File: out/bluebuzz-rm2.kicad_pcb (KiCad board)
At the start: 6 copper layers, 28 x 44 mm, 109 parts, among them J1 USB-C, J2 BAT, J3 SWD, J4 MOT, J5 TP, J6 PROBE, Q1 AO3400A, Q2 AO3400A, Q3 2N7002, SW1 PWR, U1 RP2350A, U10 USBLC6-2P6, U11 TPS22918DBVR, U2 BQ24074RGT, U20 DPS368, U21 DPS368, U22 DPS368, U23 DPS368, U24 DPS368, U3 TLV75533PDBV, U30 LSM6DS3TR-C, U5 TPS22918DBVR, U6 W25Q32JVUUIQ, U7 RM2, Y1 12MHz

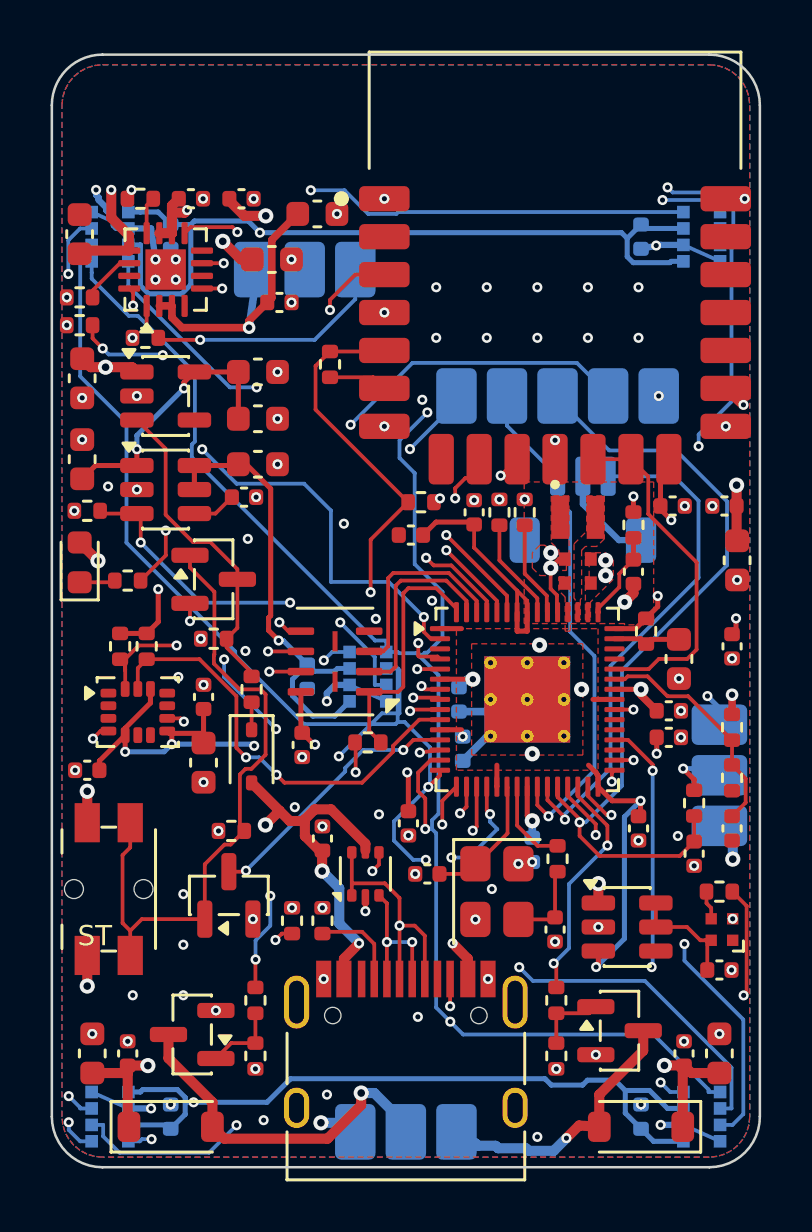
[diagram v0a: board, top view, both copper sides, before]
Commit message: Route the USB pair as one coupled pair on B.Cu
D+/D- now run 0.3 mm apart on centres (0.15 / 0.15, 90 ohm) on B.Cu over
the In4 ground, from the USB-C join vias to the vias in R3/R4; before,
freerouting split each line over F, In2 and In3. R11 and C10's GND pads,
both in the top-left sensor's no-via box, share one locked via outside
it (R11.2 was the open connection in 4 of 11 orderings).

Re-routed: 0 unconnected, 0 DRC errors, audit clean (ROUTE_FIRST=5).

Co-Authored-By: Claude Opus 5.5 <noreply@anthropic.com>
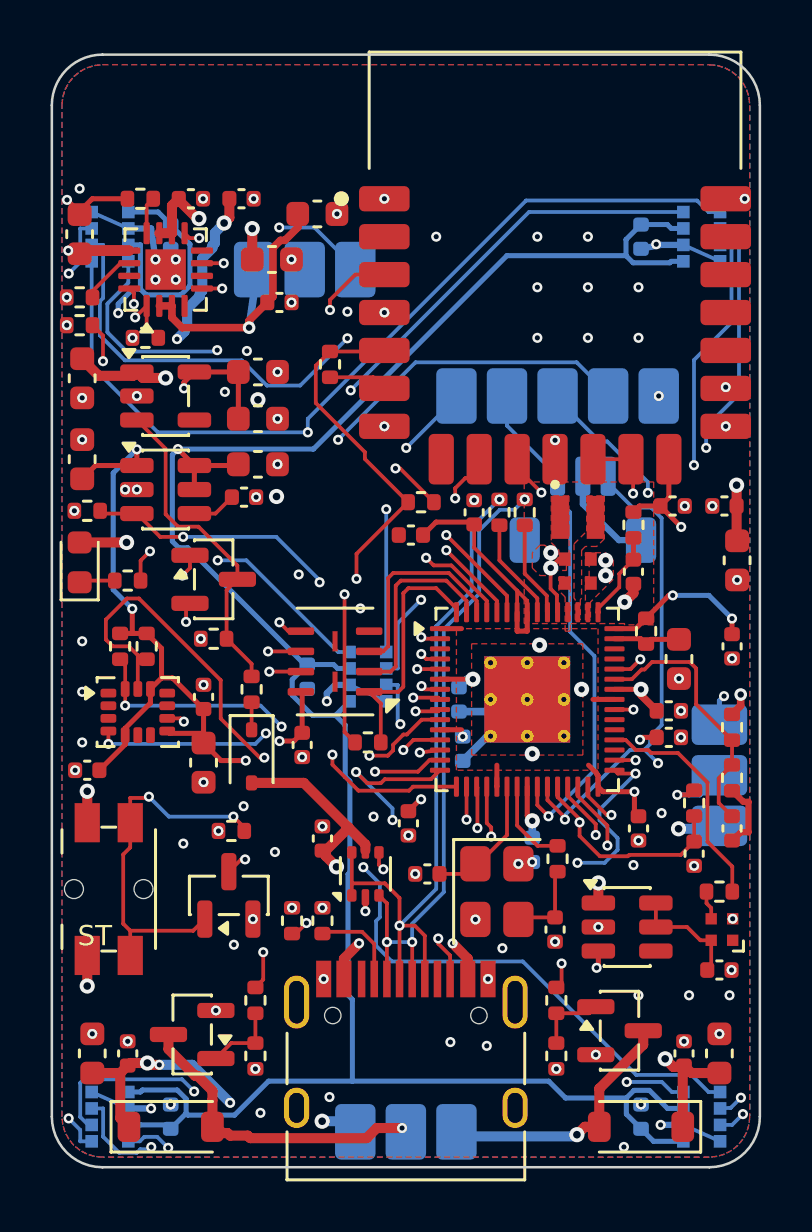
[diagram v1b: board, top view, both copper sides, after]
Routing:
- net PWR_HOLD: track 21.5 -> 31.3 mm
- net LED_STAT: track 18.4 -> 9.10 mm, vias 3 -> 0
- net 3V3_SENS: track 117.9 -> 108.9 mm, vias 3 -> 2
- net TAC_SDO: track 93.4 -> 102.2 mm, vias 8 -> 7
- net VSYS: track 33.6 -> 42.2 mm, vias 14 -> 16
- net WL_IRQ: track 4.03 -> 9.95 mm
- net TAC_SCK: track 97.7 -> 103.3 mm
- net IMU_INT1: track 19.9 -> 14.9 mm
- net SCL: track 17.3 -> 22.2 mm
- net TAC_CS5: track 18.2 -> 14.2 mm
- net TAC_CS4: track 16.9 -> 19.9 mm
- net WL_ON: track 13.7 -> 10.8 mm, vias 0 -> 2
- net RUN: track 32.1 -> 29.3 mm, vias 1 -> 2
- net 3V3_SYS: track 105.2 -> 102.4 mm, vias 17 -> 15
- net CHG_N: track 17.6 -> 15.2 mm
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
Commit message: Board rerouted with the reworked generator (ordering 42): 0 unconnected, DRC errors 0
- design.yaml routing: ordering 42 (0/0 of 48 orderings searched); a
  plain build routes that one ordering.
- stitch.py: vias for plane-net pads DRC still reports open (J5's VSYS
  test pad), and a last sweep of the vias DRC calls dangling.
- audit.py: the motor-path width rule skips wires inside a same-net pour.
- Gate evidence regenerated in design/gates/phase7/.

Co-Authored-By: Claude Opus 5.5 <noreply@anthropic.com>
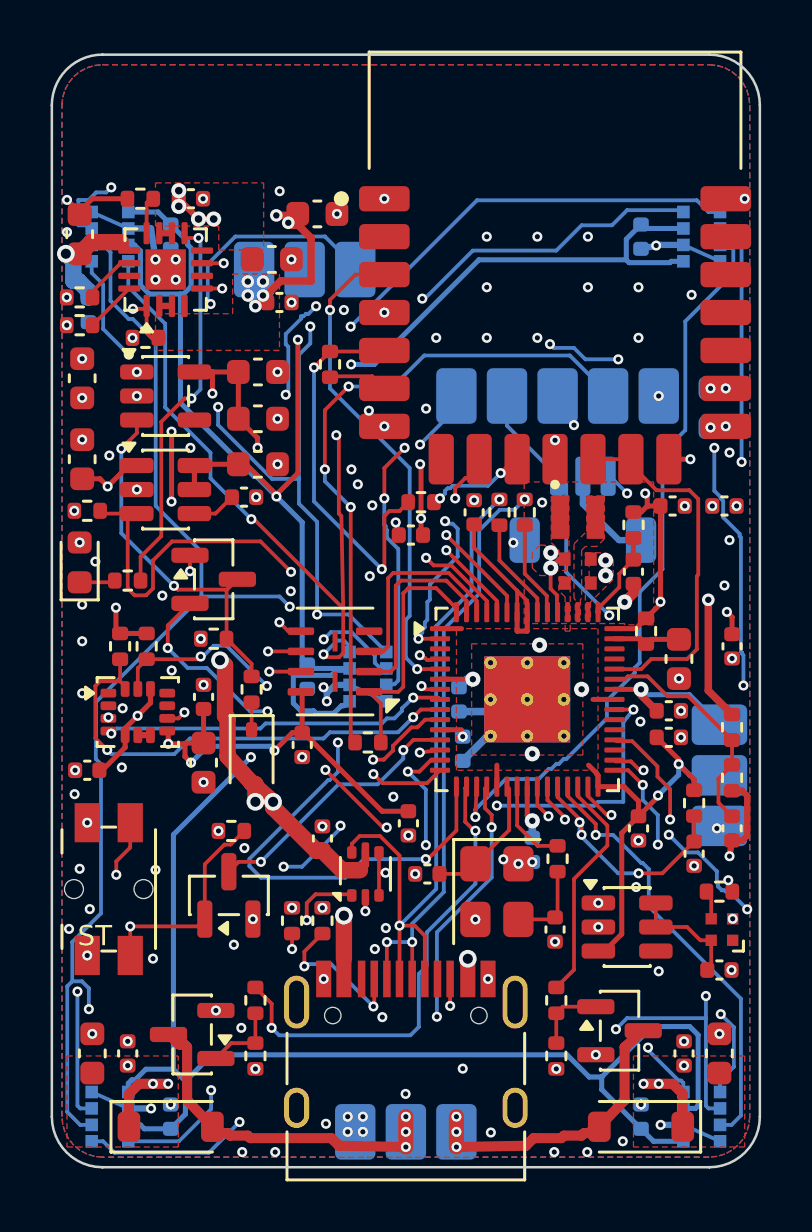
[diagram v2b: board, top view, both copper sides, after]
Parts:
- C100, C13: moved to B.Cu
- moved C13 7.48 mm to (87.5, 88.1), turned to -90 degrees
- moved C100 6.12 mm to (112.0, 92.0)
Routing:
- net TAC_CS5: track 14.2 -> 54.6 mm, vias 2 -> 9
- net VSYS: track 42.2 -> 9.05 mm, vias 16 -> 25
- net 3V3_SYS: track 102.4 -> 125.7 mm, vias 15 -> 19
- net 3V3_SENS: track 108.9 -> 126.8 mm, vias 2 -> 4
- net TAC_SDI: track 115.1 -> 124.4 mm, vias 9 -> 7
- net USB_DP: track 28.4 -> 37.0 mm, vias 2 -> 3
- net VBUS: track 63.5 -> 55.6 mm, vias 8 -> 6
- net TAC_CS2: track 37.1 -> 29.4 mm, vias 3 -> 1
- net TAC_SDO: track 102.2 -> 109.0 mm, vias 7 -> 10
- net SCL: track 22.2 -> 15.8 mm, vias 2 -> 3
- net WL_IRQ: track 9.95 -> 4.03 mm
- net SWDIO: track 41.6 -> 35.8 mm
- net USB_DM: track 29.3 -> 34.7 mm
- net SENS_EN: track 16.5 -> 20.9 mm, vias 3 -> 2
- net SDA: track 15.0 -> 19.0 mm, vias 3 -> 2
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- added copper zone on F.Cu, net VBAT
- added copper zone on F.Cu, net VSYS
